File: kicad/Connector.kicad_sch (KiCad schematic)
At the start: 14 parts, among them J2 USB_C_Receptacle_USB2.0_16P, Q4 S8050, Q5 S8050, U2 CH343G

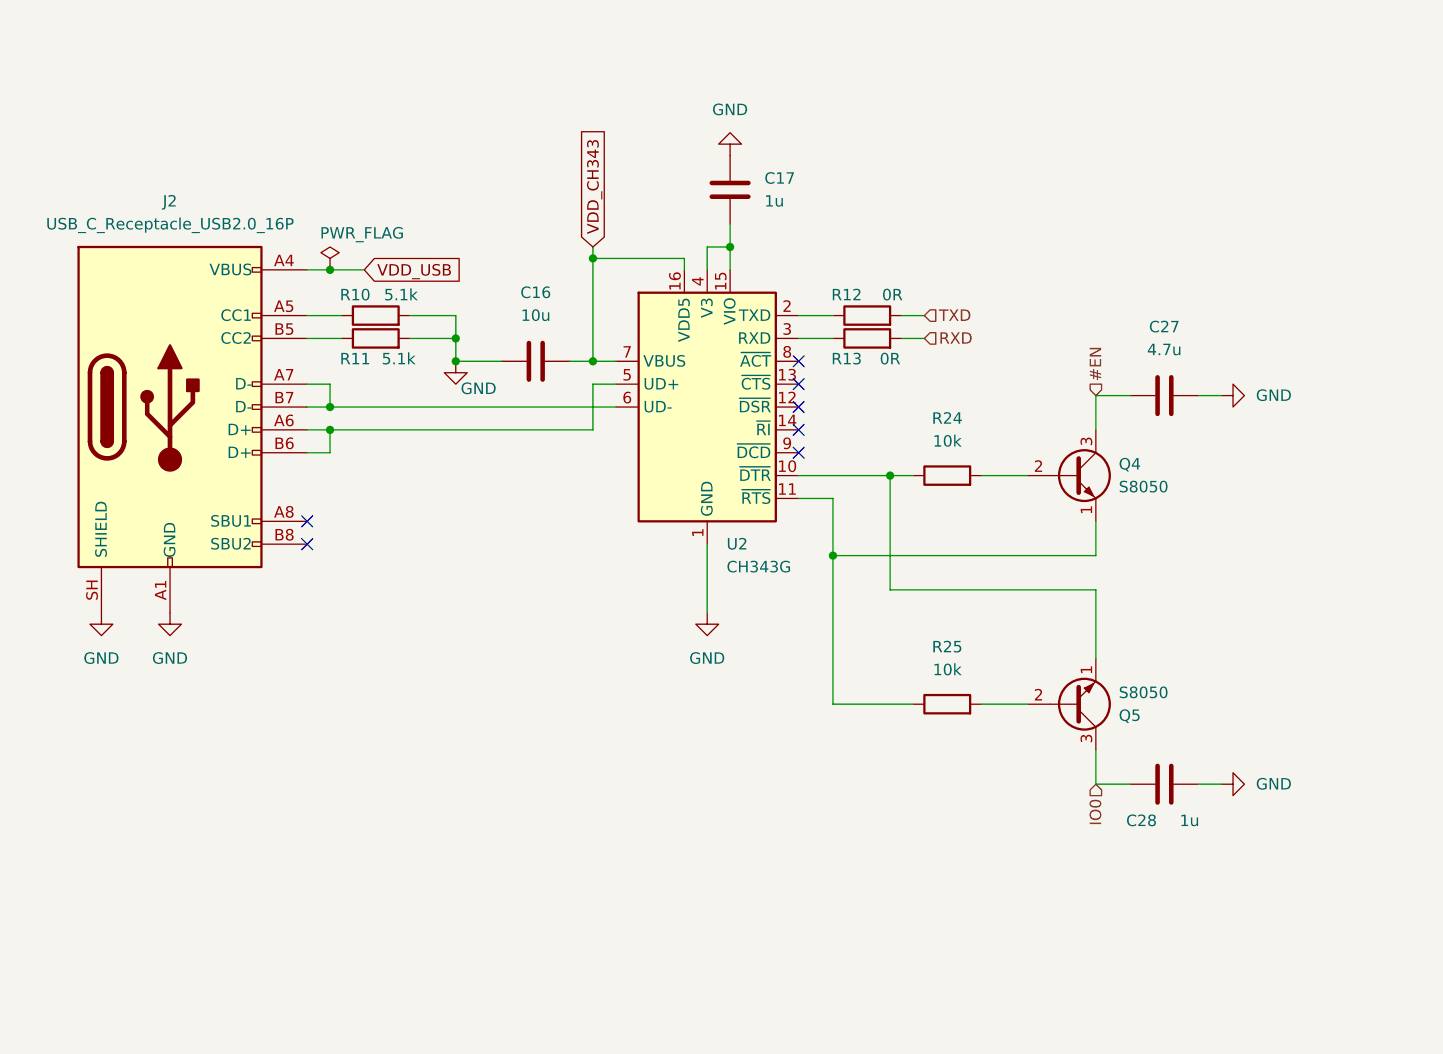
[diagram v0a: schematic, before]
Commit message: PCB updates (USB to UART circuit)
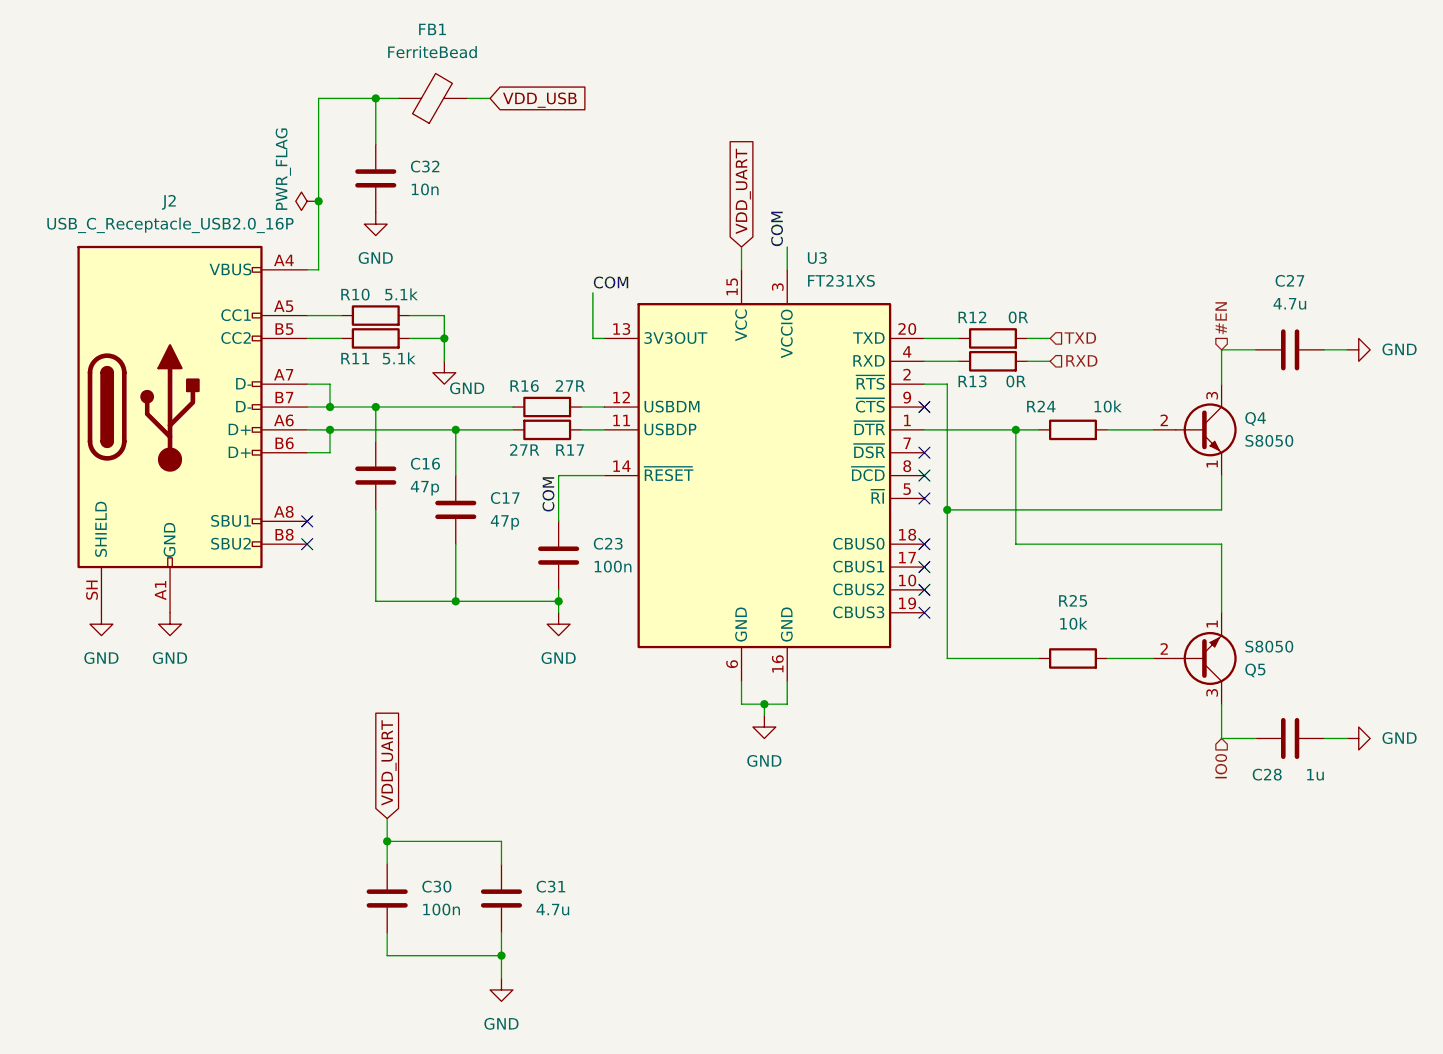
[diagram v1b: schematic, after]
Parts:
- removed U2: CH343G, Package_SO:SOIC-16_3.9x9.9mm_P1.27mm, symbol Interface_USB:CH343G
- added C23, C30: 100n, Capacitor_SMD:C_0603_1608Metric_Pad1.08x0.95mm_HandSolder, symbol Device:C
- added C31: 4.7u, Capacitor_SMD:C_0603_1608Metric_Pad1.08x0.95mm_HandSolder, symbol Device:C
- added C32: 10n, Capacitor_SMD:C_0603_1608Metric_Pad1.08x0.95mm_HandSolder, symbol Device:C
- added FB1: FerriteBead, Resistor_SMD:R_0805_2012Metric_Pad1.20x1.40mm_HandSolder, symbol Device:FerriteBead
- added R16, R17: 27R, Resistor_SMD:R_0603_1608Metric_Pad0.98x0.95mm_HandSolder, symbol Device:R
- added U3: FT231XS, Package_SO:SSOP-20_3.9x8.7mm_P0.635mm, symbol Interface_USB:FT231XS
- C16: value 10u -> 47p
- C17: value 1u -> 47p
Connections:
- net VDD_CH343 is gone; now on net GND: C16.2
- net GND: now also C17.2, C23.2, C30.2, C31.2, C32.2, U3.16 (GND), U3.6 (GND); no longer C16.1, C17.1
- net VDD_USB: now also FB1.2; no longer J2.A4 (VBUS), J2.A9 (VBUS), J2.B4 (VBUS), J2.B9 (VBUS)
- net at Q4.1 (E), R25.1: now also U3.2 (~{RTS})
- net at Q5.1 (E), R24.1: now also U3.1 (~{DTR})
- net at R12.1: now also U3.20 (TXD)
- net at R13.1: now also U3.4 (RXD)
- net at J2.A6 (D+), J2.B6 (D+): now also C17.1, R17.2
- net at J2.A7 (D-), J2.B7 (D-): now also C16.1, R16.1
- new net: R17.1, U3.11 (USBDP)
- new net: R16.2, U3.12 (USBDM)
- new net: C32.1, FB1.1, J2.A4 (VBUS), J2.A9 (VBUS), J2.B4 (VBUS), J2.B9 (VBUS)
- new net COM: C23.1, U3.13 (3V3OUT), U3.14 (~{RESET}), U3.3 (VCCIO)
- new net VDD_UART: C30.1, C31.1, U3.15 (VCC)
- no-connect marks 7 -> 10
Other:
- moved on the sheet: C27, C28, Q4, Q5, R12, R13, R24, R25
